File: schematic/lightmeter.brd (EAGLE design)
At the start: 26.7 x 38.6 mm, 91 parts, among them J1 CONNECTEDJUMPER, J2 CONNECTEDJUMPER, J3 CONNECTEDJUMPER, J4 CONNECTEDJUMPER, J5 CONNECTEDJUMPER, J6 CONNECTEDJUMPER, J7 CONNECTEDJUMPER, Q1 PCHANNELMOSFETSOT-523-3-BTTM, Y1 8MHz

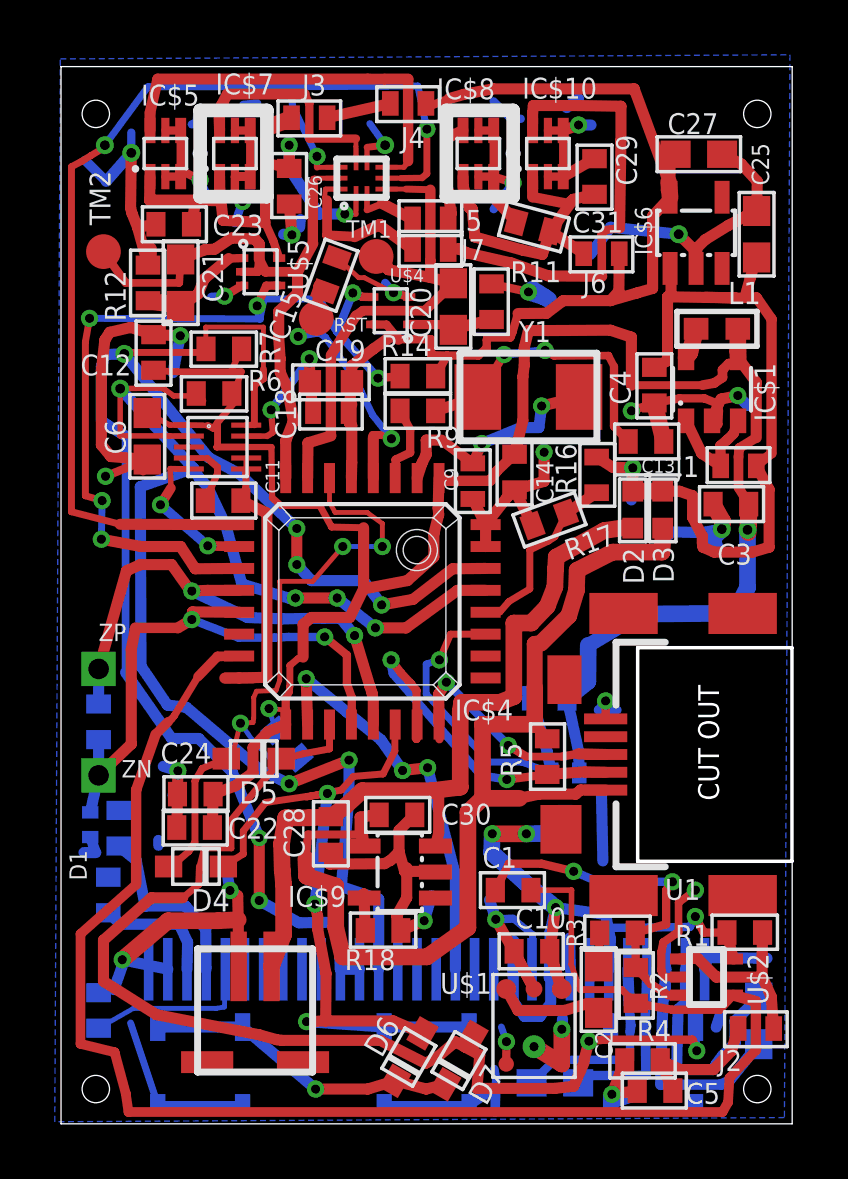
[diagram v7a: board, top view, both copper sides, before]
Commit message: Some more (incomplete) work on ground plane connectivity.
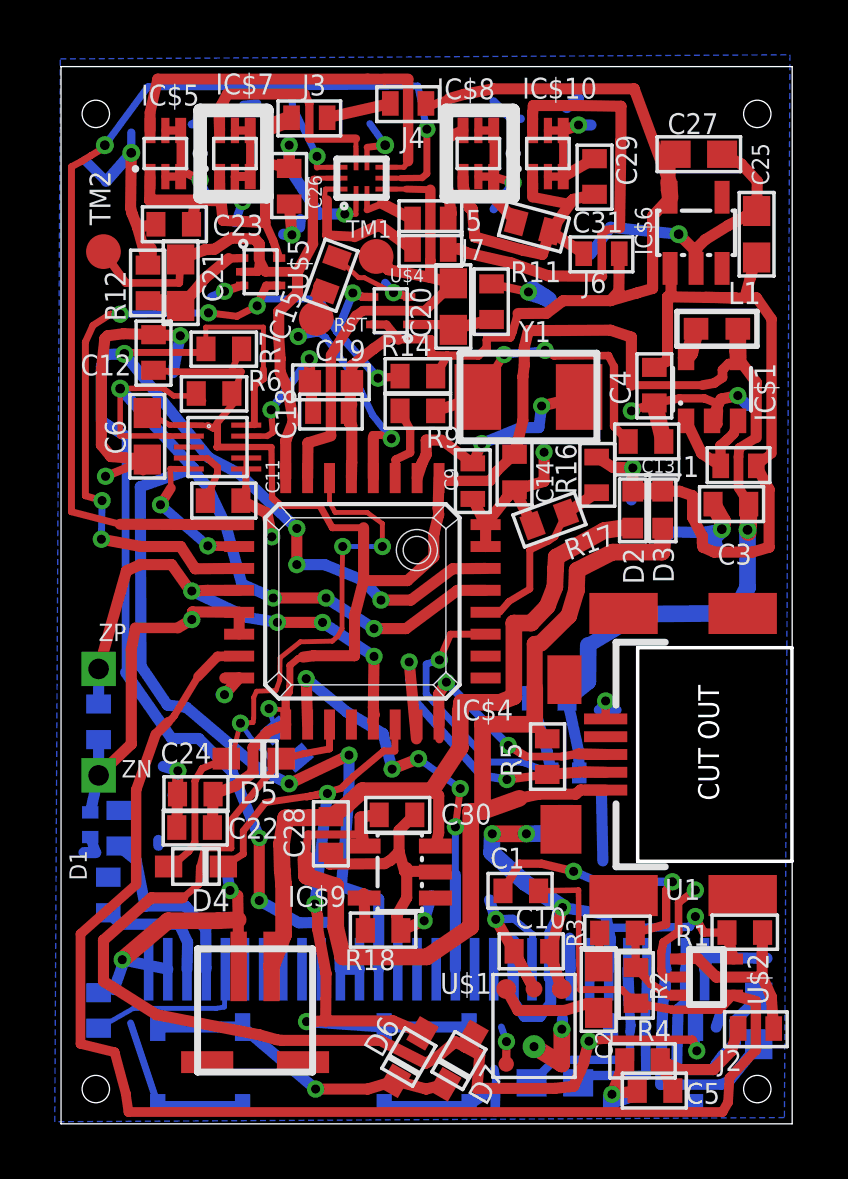
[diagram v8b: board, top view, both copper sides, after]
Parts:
- moved C1 0.28 mm to (18.1, 9.91)
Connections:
- net PIEZONEG: now also IC$4.14; no longer IC$4.20
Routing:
- net PIEZONEG: track 21.3 -> 13.5 mm, vias 2 -> 1
- net GND: track 172.4 -> 167.3 mm, vias 29 -> 31
- net INTEGCLR: track 31.5 -> 30.0 mm, vias 6 -> 7
- net SCRRES: track 15.0 -> 16.0 mm, vias 3 -> 5
- net SWDIO/USBD-: track 13.9 -> 13.1 mm
- net VBAT: track 28.6 -> 28.0 mm
- net PIEZOPOS: track 19.5 -> 19.4 mm, vias 2 -> 4
